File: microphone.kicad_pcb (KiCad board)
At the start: 2 copper layers, 21 parts, among them U1 NMA0515SC

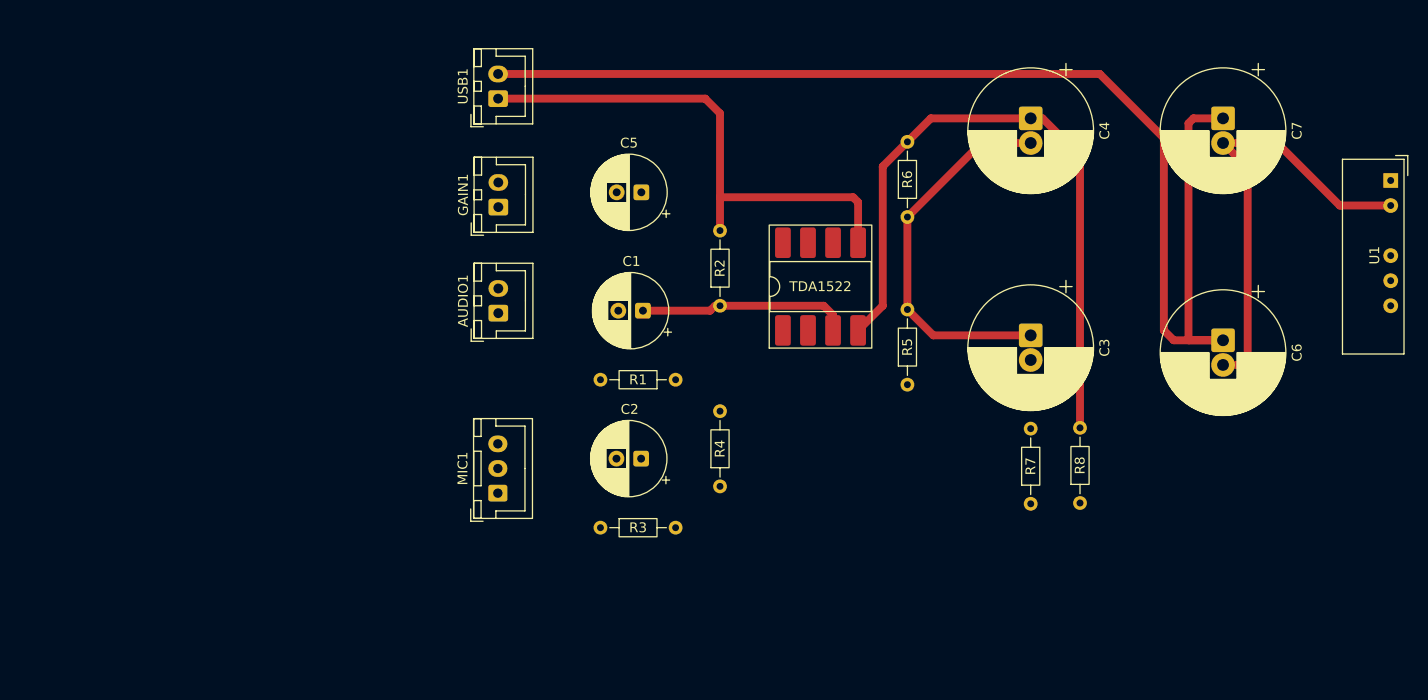
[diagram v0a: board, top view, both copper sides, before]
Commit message: Add Mounting Hole symbols and update references in schematic - Created a new design rule file (DRU) with custom DRC settings for PCBWay
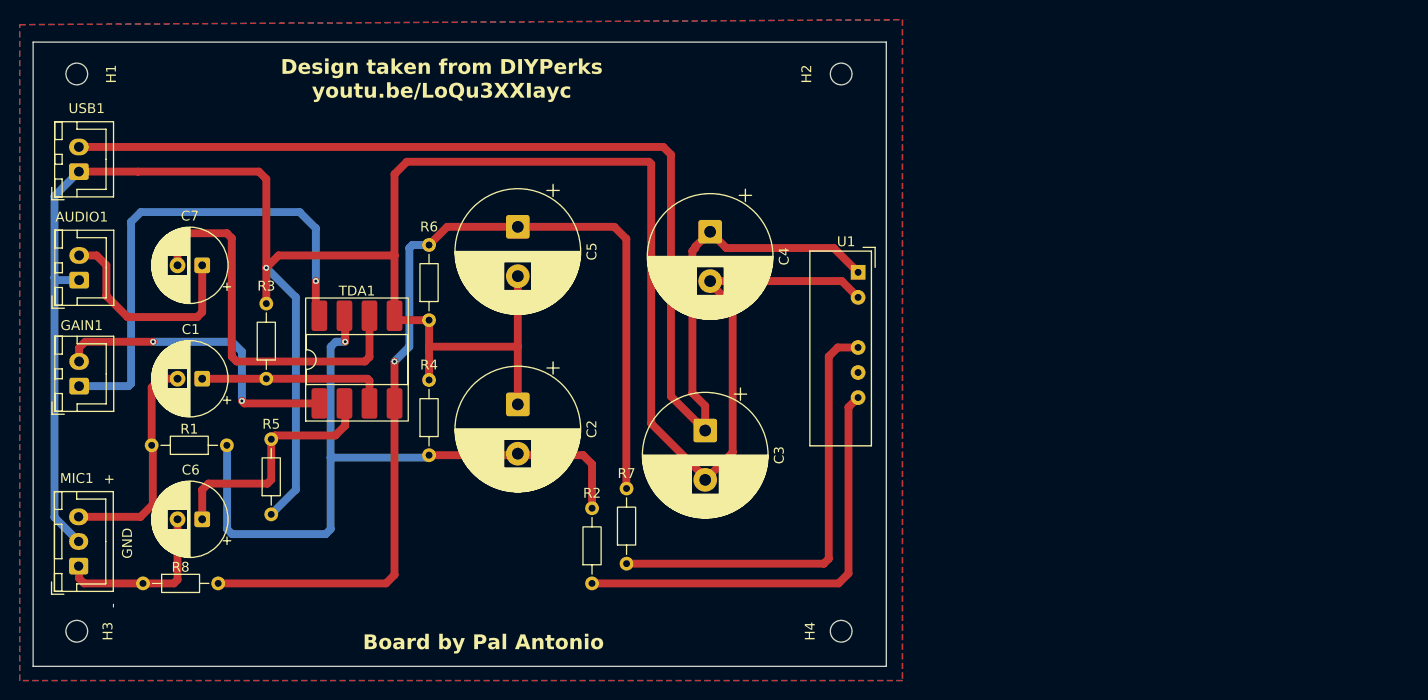
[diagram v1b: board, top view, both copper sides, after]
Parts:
- added H1: MountingHole, MountingHole:MountingHole_2.2mm_M2, F.Cu at (32.8, 22.5)
- added H2: MountingHole, MountingHole:MountingHole_2.2mm_M2, F.Cu at (110.3, 22.5)
- added H3: MountingHole, MountingHole:MountingHole_2.2mm_M2, F.Cu at (32.8, 79.0)
- added H4: MountingHole, MountingHole:MountingHole_2.2mm_M2, F.Cu at (110.3, 79.0)
- C2: renamed from C3; footprint Capacitor_THT:CP_Radial_D12.5mm_P2.50mm -> Capacitor_THT:CP_Radial_D12.5mm_P5.00mm
- C3: renamed from C6; footprint Capacitor_THT:CP_Radial_D12.5mm_P2.50mm -> Capacitor_THT:CP_Radial_D12.5mm_P5.00mm
- C4: renamed from C7; footprint Capacitor_THT:CP_Radial_D12.5mm_P2.50mm -> Capacitor_THT:CP_Radial_D12.5mm_P5.00mm
- C5: renamed from C4; footprint Capacitor_THT:CP_Radial_D12.5mm_P2.50mm -> Capacitor_THT:CP_Radial_D12.5mm_P5.00mm
- moved U1 54.8 mm to (112.0, 42.6)
- moved C3 53.3 mm to (96.5, 58.6)
- moved C4 53.3 mm to (97.0, 38.5)
- moved C5 53.2 mm to (77.5, 38.0)
- moved C2 52.5 mm to (77.5, 56.0)
- moved R6 49.6 mm to (68.5, 47.5)
- moved R4 49.0 mm to (68.5, 61.1)
- moved TDA1 47.6 mm to (61.2, 51.5)
- moved R8 46.7 mm to (39.5, 74.2)
- moved R3 46.6 mm to (52.0, 53.4)
- moved R7 46.4 mm to (88.5, 72.2)
- moved GAIN1 46.2 mm to (33.0, 54.1)
- moved R1 46.0 mm to (48.0, 60.1)
- moved R5 45.6 mm to (52.5, 67.2)
- moved C1 45.2 mm to (45.5, 53.4)
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- renumbered C2 to C6, C5 to C7, R7 to R2, R2 to R3, R5 to R4, R4 to R5, R8 to R7, R3 to R8, TDA1522 to TDA1
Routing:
- net Net-(AUDIO1-Pin_1): track 137.3 -> 260.2 mm, vias 0 -> 1
- net Net-(TDA1-V+): track 0.00 -> 73.7 mm, vias 0 -> 1
- net Net-(GAIN1-Pin_1): track 0.00 -> 50.8 mm, vias 0 -> 1
- net Net-(U1-VOUT+): track 0.00 -> 44.7 mm
- net Net-(U1-VOUT-): track 0.00 -> 44.6 mm
- net Net-(TDA1-GND): track 0.00 -> 39.2 mm
- net Net-(TDA1-SYM): track 68.8 -> 100.7 mm, vias 0 -> 1
- net Net-(GAIN1-Pin_2): track 0.00 -> 31.5 mm, vias 0 -> 2
- net Net-(TDA1-E+): track 0.00 -> 24.9 mm
- net Net-(MIC1-Pin_3): track 0.00 -> 23.0 mm
- net Net-(AUDIO1-Pin_2): track 0.00 -> 21.8 mm
- net Net-(MIC1-Pin_1): track 0.00 -> 17.7 mm
- net Net-(U1-VIN+): track 125.3 -> 127.9 mm
- net Net-(TDA1-E-): track 21.4 -> 19.3 mm
- added copper zone on B.Cu, net (none)
- added copper zone on F.Cu, net (none)
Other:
- board outline added: 86.5 x 63.3 mm
- board text added: "+"
- board text added: "-"
- board text added: "Board by Pal Antonio"
- board text added: "Design taken from DIYPerks youtu.be/LoQu3XXIayc"
- board text added: "GND"
